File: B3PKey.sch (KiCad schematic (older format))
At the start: 178 parts, among them SW1 SW_Push, U1 ATmega32U4-AU, Y1 16MHz

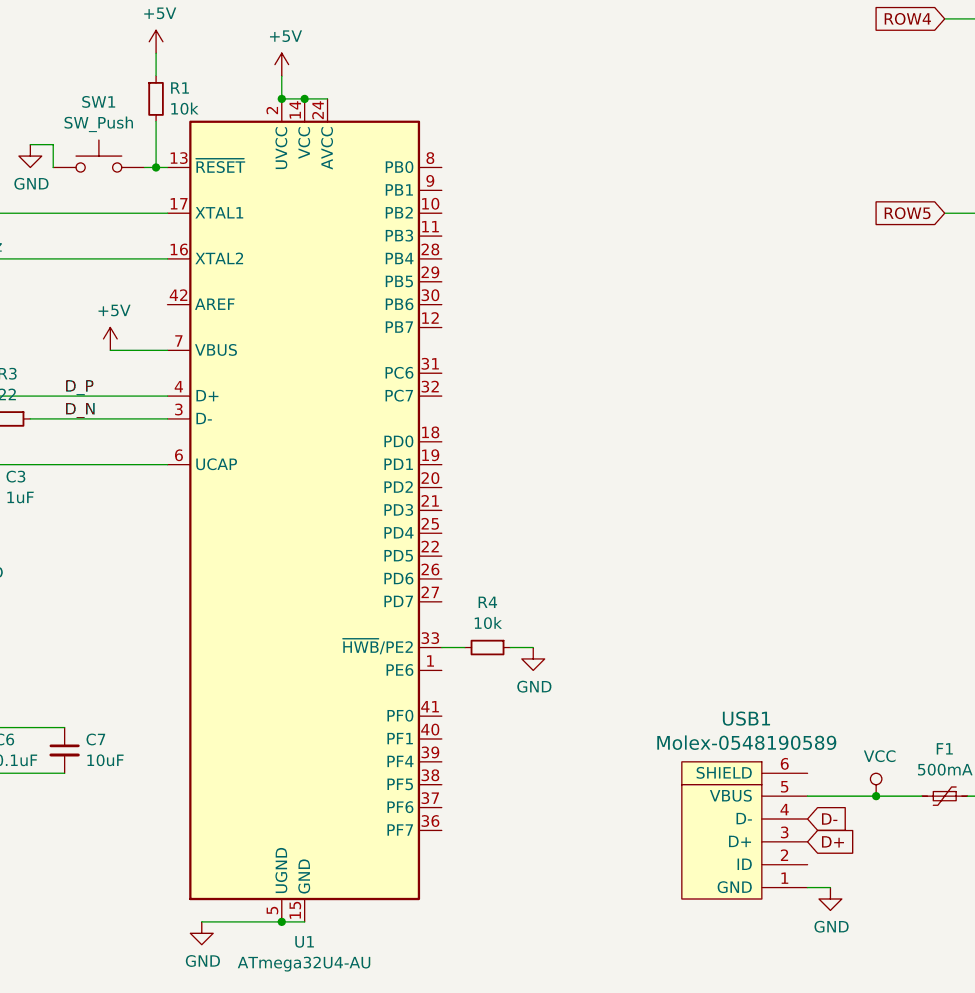
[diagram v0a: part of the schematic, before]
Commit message: Move components to forehead and route all traces
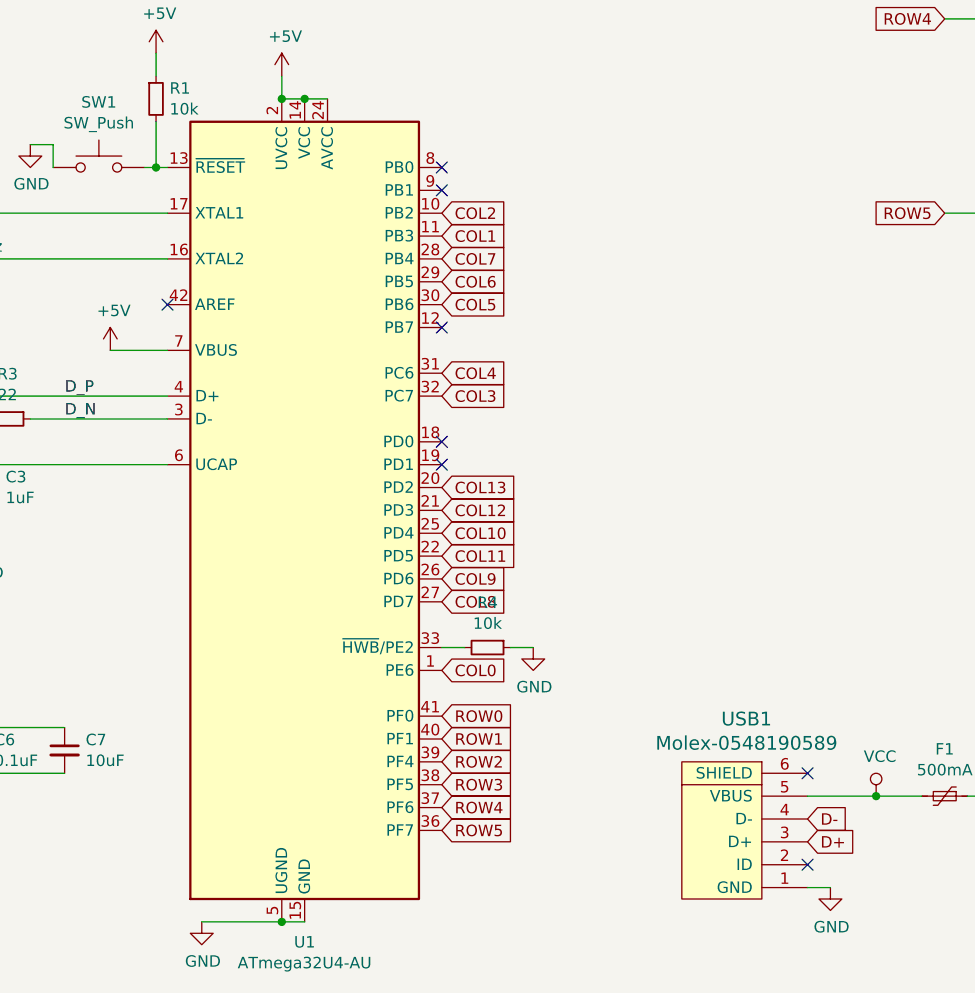
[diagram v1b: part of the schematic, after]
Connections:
- net COL0: now also U1.1 (PE6)
- net COL1: now also U1.11 (PB3)
- net COL10: now also U1.25 (PD4)
- net COL11: now also U1.22 (PD5)
- net COL12: now also U1.21 (PD3)
- net COL13: now also U1.20 (PD2)
- net COL2: now also U1.10 (PB2)
- net COL3: now also U1.32 (PC7)
- net COL4: now also U1.31 (PC6)
- net COL5: now also U1.30 (PB6)
- net COL6: now also U1.29 (PB5)
- net COL7: now also U1.28 (PB4)
- net COL8: now also U1.27 (PD7)
- net COL9: now also U1.26 (PD6)
- net ROW0: now also U1.41 (PF0)
- net ROW1: now also U1.40 (PF1)
- net ROW2: now also U1.39 (PF4)
- net ROW3: now also U1.38 (PF5)
- net ROW4: now also U1.37 (PF6)
- net ROW5: now also U1.36 (PF7)
- no-connect marks 0 -> 8
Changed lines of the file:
@@
 Text Label 2050 8600 0    50   ~ 0
 D_N
+Text GLabel 3700 8500 2    50   Input ~ 0
+COL3
+Text GLabel 3700 8400 2    50   Input ~ 0
+COL4
+Text GLabel 3700 8100 2    50   Input ~ 0
+COL5
+Text GLabel 3700 8000 2    50   Input ~ 0
+COL6
+Text GLabel 3700 7900 2    50   Input ~ 0
+COL7
+Text GLabel 3700 9400 2    50   Input ~ 0
+COL8
+Text GLabel 3700 9300 2    50   Input ~ 0
+COL9
+Text GLabel 3700 9100 2    50   Input ~ 0
+COL10
+Text GLabel 3700 8900 2    50   Input ~ 0
+COL13
+Text GLabel 3700 9000 2    50   Input ~ 0
+COL12
+Text GLabel 3700 9200 2    50   Input ~ 0
+COL11
+Text GLabel 3700 9900 2    50   Input ~ 0
+ROW0
+Text GLabel 3700 10000 2    50   Input ~ 0
+ROW1
+Text GLabel 3700 10100 2    50   Input ~ 0
+ROW2
+Text GLabel 3700 10200 2    50   Input ~ 0
+ROW3
+Text GLabel 3700 10300 2    50   Input ~ 0
+ROW4
+Text GLabel 3700 10400 2    50   Input ~ 0
+ROW5
+NoConn ~ 2500 8100
+Text GLabel 3700 9700 2    50   Input ~ 0
+COL0
+NoConn ~ 3700 7500
+NoConn ~ 3700 7600
+NoConn ~ 3700 8200
+NoConn ~ 3700 8700
+NoConn ~ 3700 8800
+NoConn ~ 5300 10150
+NoConn ~ 5300 10550
+Text GLabel 3700 7800 2    50   Input ~ 0
+COL1
+Text GLabel 3700 7700 2    50   Input ~ 0
+COL2
 $EndSCHEMATC

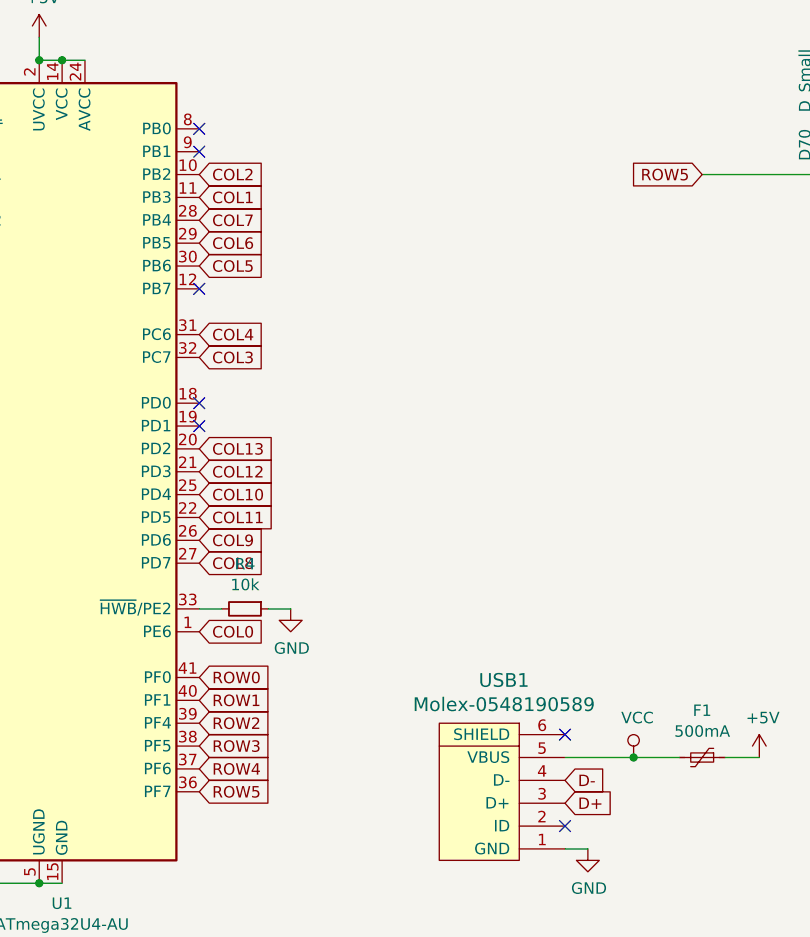
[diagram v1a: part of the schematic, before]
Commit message: Rotate controller and reroute traces
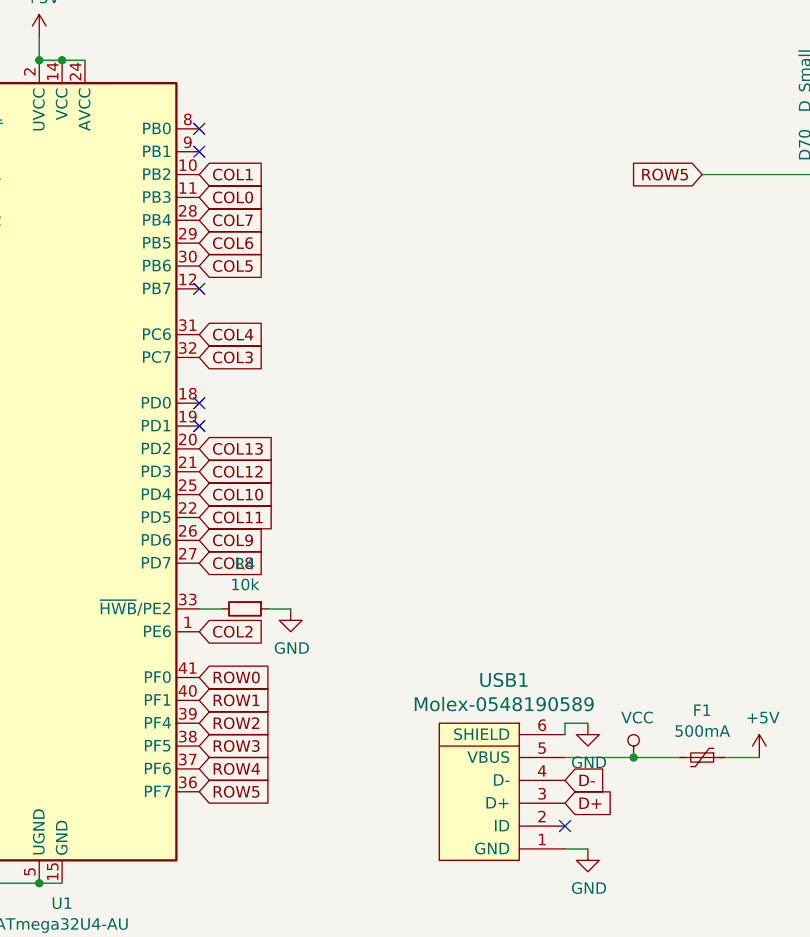
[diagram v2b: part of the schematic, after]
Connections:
- net COL0: now also U1.11 (PB3); no longer U1.1 (PE6)
- net COL1: now also U1.10 (PB2); no longer U1.11 (PB3)
- net COL2: now also U1.1 (PE6); no longer U1.10 (PB2)
- net GND: now also USB1.6 (SHIELD)
- no-connect marks 8 -> 7
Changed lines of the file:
@@
 ROW5
 NoConn ~ 2500 8100
-Text GLabel 3700 9700 2    50   Input ~ 0
+Text GLabel 3700 7800 2    50   Input ~ 0
 COL0
 NoConn ~ 3700 7500
@@
 NoConn ~ 3700 8700
 NoConn ~ 3700 8800
-NoConn ~ 5300 10150
 NoConn ~ 5300 10550
-Text GLabel 3700 7800 2    50   Input ~ 0
+Text GLabel 3700 9700 2    50   Input ~ 0
+COL2
+Text GLabel 3700 7700 2    50   Input ~ 0
 COL1
-Text GLabel 3700 7700 2    50   Input ~ 0
-COL2
+$Comp
+L power:GND #PWR0101
+U 1 1 5F3A9AAF
+P 5400 10100
+F 0 "#PWR0101" H 5400 9850 50  0001 C CNN
+F 1 "GND" H 5405 9927 50  0000 C CNN
+F 2 "" H 5400 10100 50  0001 C CNN
+F 3 "" H 5400 10100 50  0001 C CNN
+	1    5400 10100
+	1    0    0    -1
+$EndComp
+Wire Wire Line
+	5300 10150 5300 10100
+Wire Wire Line
+	5300 10100 5400 10100
 $EndSCHEMATC

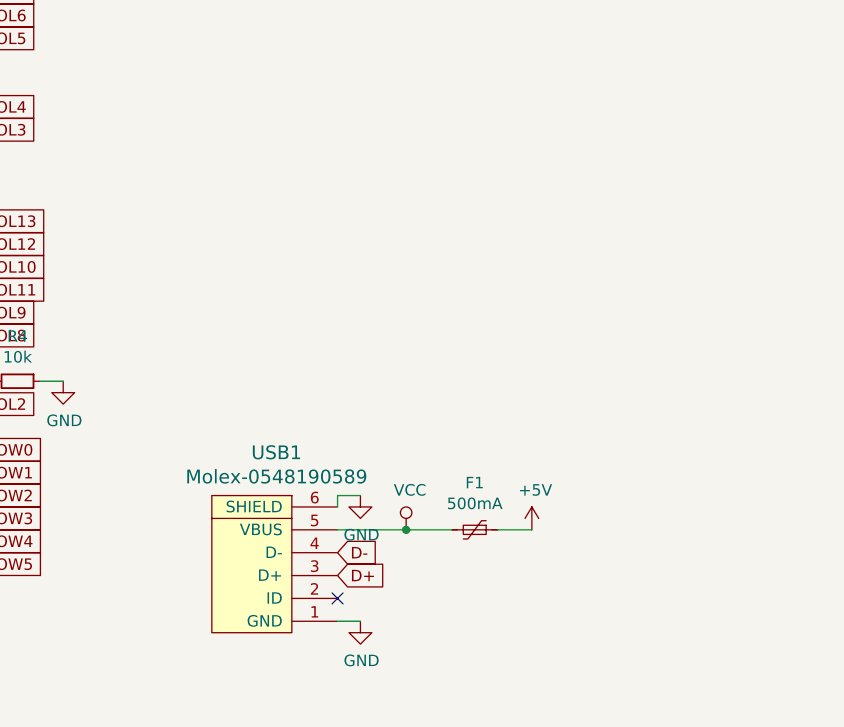
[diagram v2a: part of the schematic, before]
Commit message: Change to USB Type-C
Changed the board to use a USB Type-C connector, added required components and modified ground plane to be neater. Also generated OUTDATED Gerber files.

TODO: Generate new Gerbers
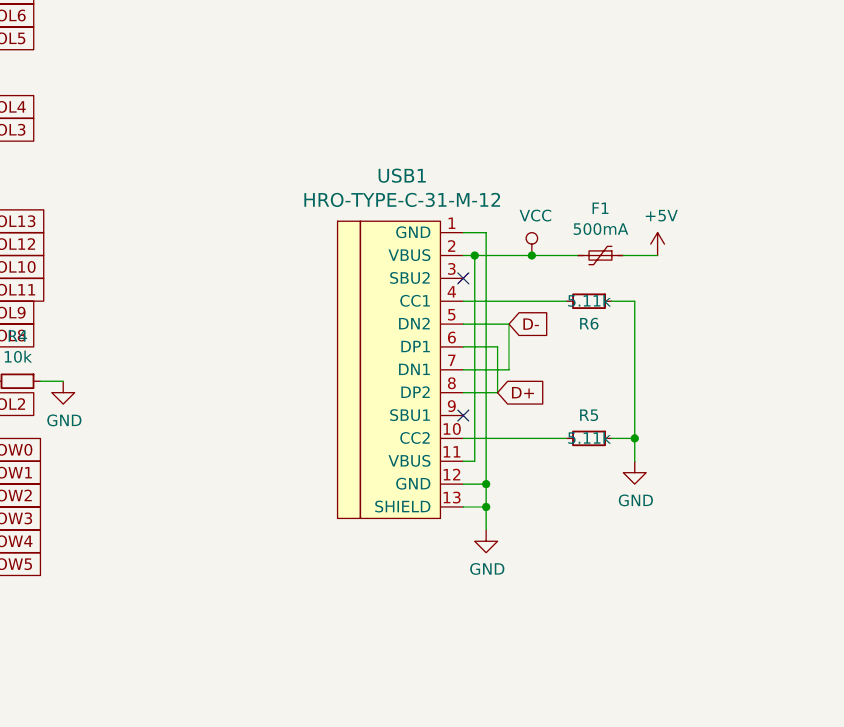
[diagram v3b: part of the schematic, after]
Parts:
- removed USB1: Molex-0548190589, random-keyboard-parts:Molex-0548190589, symbol random-keyboard-parts:Molex-0548190589
- added R5, R6: 5.11k, Resistor_SMD:R_0805_2012Metric, symbol Device:R_Small
- added USB1: HRO-TYPE-C-31-M-12, Type-C:HRO-TYPE-C-31-M-12-HandSoldering, symbol Type-C:HRO-TYPE-C-31-M-12
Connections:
- net D+: now also USB1.6 (DP1), USB1.8 (DP2)
- net D-: now also USB1.5 (DN2), USB1.7 (DN1)
- net GND: now also R5.1, R6.1, USB1.1 (GND), USB1.12 (GND), USB1.13 (SHIELD)
- net VCC: now also USB1.11 (VBUS), USB1.2 (VBUS)
- new net: R5.2, USB1.10 (CC2)
- new net: R6.2, USB1.4 (CC1)
- no-connect marks 7 -> 8
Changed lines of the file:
@@
 Wire Wire Line
 	2450 7100 2450 7000
-$Comp
-L random-keyboard-parts:Molex-0548190589 USB1
-U 1 1 5F2FBE50
-P 5000 10450
-F 0 "USB1" V 5537 10417 60  0000 C CNN
-F 1 "Molex-0548190589" V 5431 10417 60  0000 C CNN
-F 2 "random-keyboard-parts:Molex-0548190589" H 5000 10450 60  0001 C CNN
-F 3 "" H 5000 10450 60  0001 C CNN
-	1    5000 10450
-	0    -1   -1   0
-$EndComp
-$Comp
-L power:VCC #PWR010
-U 1 1 5F329948
-P 5600 10250
-F 0 "#PWR010" H 5600 10100 50  0001 C CNN
-F 1 "VCC" H 5617 10423 50  0000 C CNN
-F 2 "" H 5600 10250 50  0001 C CNN
-F 3 "" H 5600 10250 50  0001 C CNN
-	1    5600 10250
-	1    0    0    -1
-$EndComp
-$Comp
-L Device:Polyfuse_Small F1
-U 1 1 5F32A16A
-P 5900 10250
-F 0 "F1" V 5695 10250 50  0000 C CNN
-F 1 "500mA" V 5786 10250 50  0000 C CNN
-F 2 "Fuse:Fuse_0805_2012Metric" H 5950 10050 50  0001 L CNN
-F 3 "~" H 5900 10250 50  0001 C CNN
-	1    5900 10250
-	0    1    1    0
-$EndComp
-$Comp
-L power:+5V #PWR011
-U 1 1 5F32A73A
-P 6150 10250
-F 0 "#PWR011" H 6150 10100 50  0001 C CNN
-F 1 "+5V" H 6165 10423 50  0000 C CNN
-F 2 "" H 6150 10250 50  0001 C CNN
-F 3 "" H 6150 10250 50  0001 C CNN
-	1    6150 10250
-	1    0    0    -1
-$EndComp
-Wire Wire Line
-	5300 10250 5600 10250
-Wire Wire Line
-	5600 10250 5800 10250
-Connection ~ 5600 10250
-Wire Wire Line
-	6000 10250 6150 10250
-Text GLabel 5300 10350 2    50   Input ~ 0
+Text GLabel 6050 9350 2    50   Input ~ 0
 D-
-Text GLabel 5300 10450 2    50   Input ~ 0
+Text GLabel 6000 9650 2    50   Input ~ 0
 D+
-$Comp
-L power:GND #PWR012
-U 1 1 5F32E827
-P 5400 10650
-F 0 "#PWR012" H 5400 10400 50  0001 C CNN
-F 1 "GND" H 5405 10477 50  0000 C CNN
-F 2 "" H 5400 10650 50  0001 C CNN
-F 3 "" H 5400 10650 50  0001 C CNN
-	1    5400 10650
-	1    0    0    -1
-$EndComp
-Wire Wire Line
-	5300 10650 5400 10650
 Connection ~ 13800 4650
 Connection ~ 13250 4650
@@
 NoConn ~ 3700 8700
 NoConn ~ 3700 8800
-NoConn ~ 5300 10550
 Text GLabel 3700 9700 2    50   Input ~ 0
 COL2
 Text GLabel 3700 7700 2    50   Input ~ 0
 COL1
+Wire Wire Line
+	6550 9050 6700 9050
+Connection ~ 6150 9050
+Wire Wire Line
+	6150 9050 6350 9050
+Wire Wire Line
+	5850 9050 5900 9050
+$Comp
+L power:+5V #PWR0102
+U 1 1 5F3F9081
+P 6700 9050
+F 0 "#PWR0102" H 6700 8900 50  0001 C CNN
+F 1 "+5V" H 6715 9223 50  0000 C CNN
+F 2 "" H 6700 9050 50  0001 C CNN
+F 3 "" H 6700 9050 50  0001 C CNN
+	1    6700 9050
+	1    0    0    -1
+$EndComp
+$Comp
+L Device:Polyfuse_Small F1
+U 1 1 5F3F9087
+P 6450 9050
+F 0 "F1" V 6245 9050 50  0000 C CNN
+F 1 "500mA" V 6336 9050 50  0000 C CNN
+F 2 "Fuse:Fuse_0805_2012Metric" H 6500 8850 50  0001 L CNN
+F 3 "~" H 6450 9050 50  0001 C CNN
+	1    6450 9050
+	0    1    1    0
+$EndComp
+$Comp
+L power:VCC #PWR0103
+U 1 1 5F3F908D
+P 6150 9050
+F 0 "#PWR0103" H 6150 8900 50  0001 C CNN
+F 1 "VCC" H 6167 9223 50  0000 C CNN
+F 2 "" H 6150 9050 50  0001 C CNN
+F 3 "" H 6150 9050 50  0001 C CNN
+	1    6150 9050
+	1    0    0    -1
+$EndComp
+$Comp
+L Device:R_Small R5
+U 1 1 5F507B1A
+P 6400 9850
+F 0 "R5" V 6300 9850 50  0000 C CNN
+F 1 "5.11k" V 6400 9850 50  0000 C CNN
+F 2 "Resistor_SMD:R_0805_2012Metric" H 6400 9850 50  0001 C CNN
+F 3 "~" H 6400 9850 50  0001 C CNN
+	1    6400 9850
+	0    1    1    0
+$EndComp
+$Comp
+L Device:R_Small R6
+U 1 1 5F508938
+P 6400 9250
+F 0 "R6" V 6500 9250 50  0000 C CNN
+F 1 "5.11k" V 6400 9250 50  0000 C CNN
+F 2 "Resistor_SMD:R_0805_2012Metric" H 6400 9250 50  0001 C CNN
+F 3 "~" H 6400 9250 50  0001 C CNN
+	1    6400 9250
+	0    1    1    0
+$EndComp
+Wire Wire Line
+	6500 9850 6600 9850
+Wire Wire Line
+	6600 9250 6500 9250
+$Comp
+L power:GND #PWR0104
+U 1 1 5F5A137F
+P 6600 9950
+F 0 "#PWR0104" H 6600 9700 50  0001 C CNN
+F 1 "GND" H 6605 9777 50  0000 C CNN
+F 2 "" H 6600 9950 50  0001 C CNN
+F 3 "" H 6600 9950 50  0001 C CNN
+	1    6600 9950
+	1    0    0    -1
+$EndComp
+$Comp
+L Type-C:HRO-TYPE-C-31-M-12 USB1
+U 1 1 5F65384D
+P 5750 9500
+F 0 "USB1" H 5583 10297 60  0000 C CNN
+F 1 "HRO-TYPE-C-31-M-12" H 5583 10191 60  0000 C CNN
+F 2 "Type-C:HRO-TYPE-C-31-M-12-HandSoldering" H 5750 9500 60  0001 C CNN
+F 3 "" H 5750 9500 60  0001 C CNN
+	1    5750 9500
+	1    0    0    -1
+$EndComp
+NoConn ~ 5850 9750
+NoConn ~ 5850 9150
+Wire Wire Line
+	5850 9950 5900 9950
+Wire Wire Line
+	5900 9950 5900 9050
+Connection ~ 5900 9050
+Wire Wire Line
+	5900 9050 6150 9050
+Wire Wire Line
+	5850 8950 5950 8950
+Wire Wire Line
+	5950 8950 5950 10050
+Wire Wire Line
+	5950 10050 5850 10050
+Wire Wire Line
+	5850 10150 5950 10150
+Wire Wire Line
+	5950 10150 5950 10250
 $Comp
 L power:GND #PWR0101
-U 1 1 5F3A9AAF
-P 5400 10100
-F 0 "#PWR0101" H 5400 9850 50  0001 C CNN
-F 1 "GND" H 5405 9927 50  0000 C CNN
-F 2 "" H 5400 10100 50  0001 C CNN
-F 3 "" H 5400 10100 50  0001 C CNN
-	1    5400 10100
-	1    0    0    -1
-$EndComp
-Wire Wire Line
-	5300 10150 5300 10100
-Wire Wire Line
-	5300 10100 5400 10100
+U 1 1 5F70B6D2
+P 5950 10250
+F 0 "#PWR0101" H 5950 10000 50  0001 C CNN
+F 1 "GND" H 5955 10077 50  0000 C CNN
+F 2 "" H 5950 10250 50  0001 C CNN
+F 3 "" H 5950 10250 50  0001 C CNN
+	1    5950 10250
+	1    0    0    -1
+$EndComp
+Wire Wire Line
+	5950 10050 5950 10150
+Connection ~ 5950 10050
+Connection ~ 5950 10150
+Wire Wire Line
+	5850 9250 6300 9250
+Wire Wire Line
+	6600 9250 6600 9850
+Wire Wire Line
+	6600 9850 6600 9950
+Connection ~ 6600 9850
+Wire Wire Line
+	5850 9850 6300 9850
+Wire Wire Line
+	5850 9450 6000 9450
+Wire Wire Line
+	6000 9450 6000 9650
+Wire Wire Line
+	6000 9650 5850 9650
+Wire Wire Line
+	5850 9350 6050 9350
+Wire Wire Line
+	6050 9350 6050 9550
+Wire Wire Line
+	6050 9550 5850 9550
 $EndSCHEMATC
